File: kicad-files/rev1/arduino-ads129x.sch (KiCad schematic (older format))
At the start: 229 parts

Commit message: choose Zener and resettable fuse values
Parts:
- D?: value ZENER -> MMSZ27T1G; footprint (none) -> SOD-123
- TH?: value Resetable Fuse -> MINIASMDC050F-2; footprint (none) -> SM1812
- TH?: value PTC -> PTS181260V014; footprint (none) -> SM1812
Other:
- moved on the sheet: TH?
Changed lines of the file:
@@
-EESchema Schematic File Version 2  date Sun 09 Jun 2013 01:11:04 PM CEST
+EESchema Schematic File Version 2  date Fri 14 Jun 2013 02:24:15 AM UTC
 LIBS:power
 LIBS:device
@@
 Sheet 1 1
 Title ""
-Date "9 jun 2013"
+Date "14 jun 2013"
 Rev ""
 Comp ""
@@
 Connection ~ 19100 1900
 Wire Wire Line
-	19250 1900 19100 1900
+	19300 1900 19100 1900
 Wire Wire Line
 	19100 1900 18850 1900
@@
 	29050 29250 29050 29850
 Wire Wire Line
-	19750 1900 19900 1900
+	19800 1900 19900 1900
 Wire Wire Line
 	38750 1800 38750 2000
@@
 P 19100 2100
 F 0 "D?" H 19100 2200 50  0000 C CNN
-F 1 "ZENER" H 19100 2000 40  0000 C CNN
+F 1 "MMSZ27T1G" H 19100 2000 40  0000 C CNN
+F 2 "SOD-123" H 19100 2100 60  0001 C CNN
 	1    19100 2100
 	0    -1   -1   0
@@
 L THERMISTOR TH?
 U 1 1 51975BAD
-P 19500 1900
-F 0 "TH?" V 19600 1950 50  0000 C CNN
-F 1 "PTC" V 19400 1900 50  0000 C CNN
-	1    19500 1900
+P 19550 1900
+F 0 "TH?" V 19650 1950 50  0000 C CNN
+F 1 "PTS181260V014" V 19450 1900 50  0000 C CNN
+F 2 "SM1812" H 19550 1900 60  0001 C CNN
+	1    19550 1900
 	0    -1   -1   0
 $EndComp
@@
 P 45550 3200
 F 0 "TH?" V 45650 3250 50  0000 C CNN
-F 1 "Resetable Fuse" V 45450 3200 50  0000 C CNN
+F 1 "MINIASMDC050F-2" V 45450 3200 50  0000 C CNN
+F 2 "SM1812" H 45550 3200 60  0001 C CNN
 	1    45550 3200
 	0    1    1    0

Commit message: Added 6V preregulator
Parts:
- added C? (x2): 100nF, symbol C
- added U?: L78L06ACUTR, SOT89, symbol 7805
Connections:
- net labels added: 6V_ISO
- wire segments 1264 -> 989
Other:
- note added: "(Limits maximum voltage if a downstream regulator fails)"
- note added: "6V PREREGULATOR"

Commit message: annotate component numbers, add power flags and NCs
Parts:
- gave numbers to parts that had none: 232
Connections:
- wire segments 989 -> 1000
- no-connect marks 6 -> 57

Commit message: hook up remaining SAM3X pins
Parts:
- added R59: R, symbol R
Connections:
- net labels removed: 5V_IN, GND_IN
- wire segments 1000 -> 1007
- no-connect marks 57 -> 58

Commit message: remove extra PWRFLAG; ERC now passes
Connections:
- wire segments 1007 -> 1006

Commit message: replace preregulator with crowbar circuits
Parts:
- removed U4: L78L06ACUTR, SOT89, symbol 7805
- added 10k1, R64: 10k, symbol R
- added R60, R61: 68, symbol R
- added R62: 19.6k, symbol R
- added R63: 8.45k, symbol R
- added U14, U4: BT1308W-600D, symbol TRIAC
- added U15, U16: TL431BIDBZR, symbol TL431LP
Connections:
- net labels removed: 6V_ISO
- wire segments 1006 -> 1028
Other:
- note added: "3.8V Crowbar circuit"
- note added: "5.5V Crowbar circuit"
- note removed: "(Limits maximum voltage if a downstream regulator fails)"
- note removed: "6V PREREGULATOR"
- moved on the sheet: C41, C42, C44, C45, C49, C52, C54, C56, C57, C58, C59, C62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

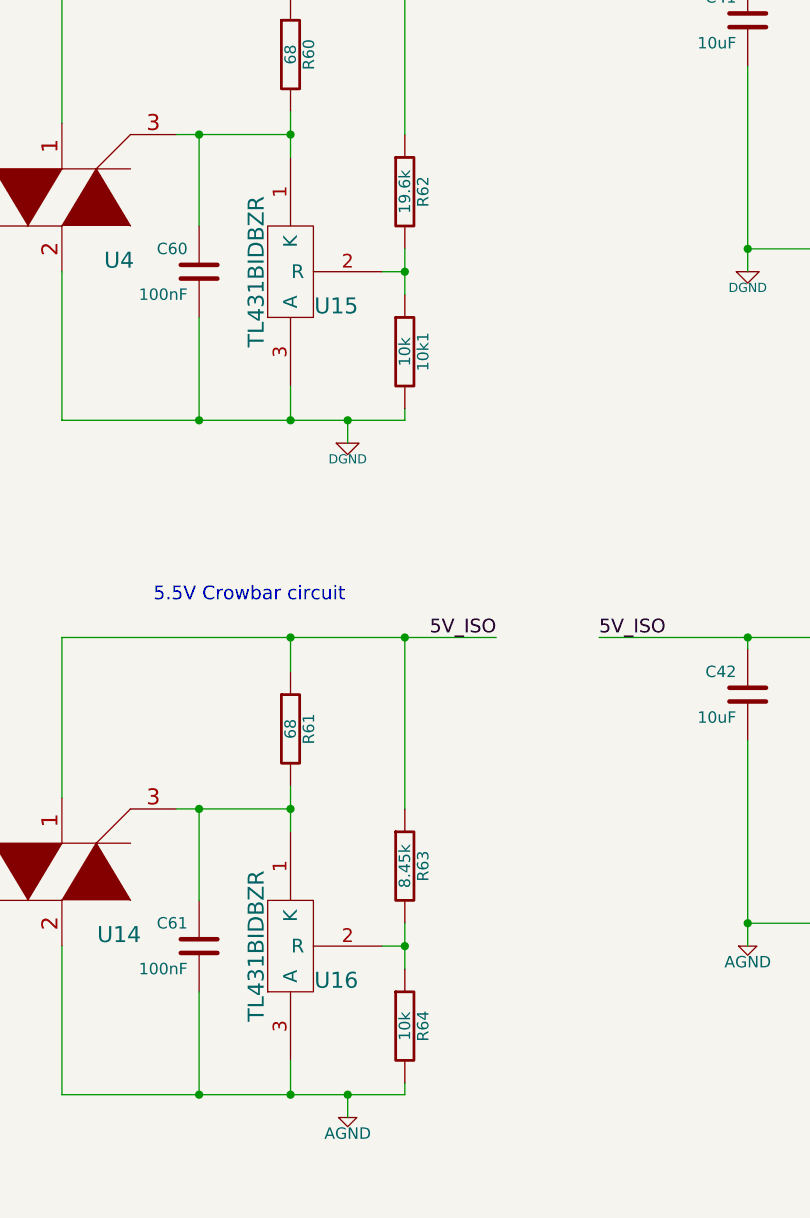
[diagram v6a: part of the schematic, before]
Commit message: swap resistors in crowbar circuits
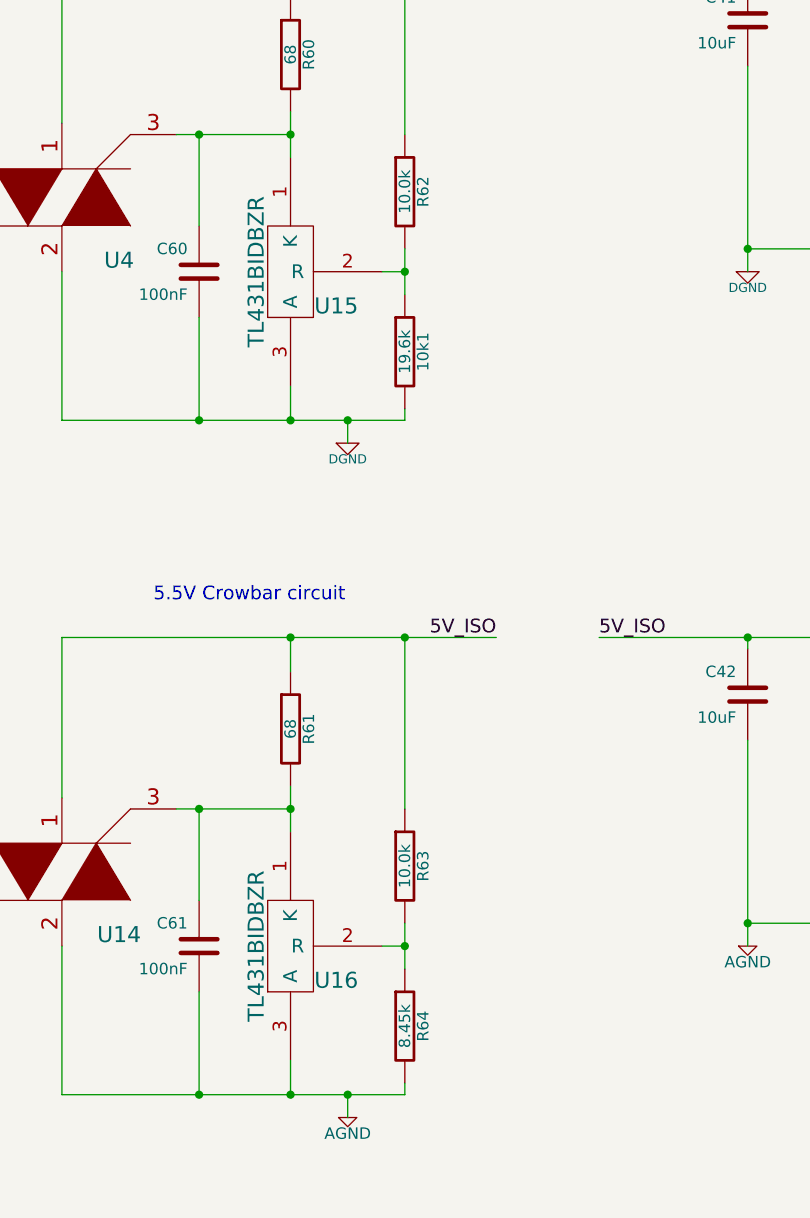
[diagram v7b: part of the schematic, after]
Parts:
- 10k1: value 10k -> 19.6k
- R62: value 19.6k -> 10.0k
- R63: value 8.45k -> 10.0k
- R64: value 10k -> 8.45k
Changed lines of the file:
@@
-EESchema Schematic File Version 2  date Sat 15 Jun 2013 02:21:45 AM UTC
+EESchema Schematic File Version 2  date Sat 15 Jun 2013 03:09:59 AM UTC
 LIBS:power
 LIBS:device
@@
 P 16100 6450
 F 0 "R62" V 16180 6450 50  0000 C CNN
-F 1 "19.6k" V 16100 6450 50  0000 C CNN
+F 1 "10.0k" V 16100 6450 50  0000 C CNN
 	1    16100 6450
 	1    0    0    -1
@@
 P 16100 7150
 F 0 "10k1" V 16180 7150 50  0000 C CNN
-F 1 "10k" V 16100 7150 50  0000 C CNN
+F 1 "19.6k" V 16100 7150 50  0000 C CNN
 	1    16100 7150
 	1    0    0    -1
@@
 P 16100 10100
 F 0 "R64" V 16180 10100 50  0000 C CNN
-F 1 "10k" V 16100 10100 50  0000 C CNN
+F 1 "8.45k" V 16100 10100 50  0000 C CNN
 	1    16100 10100
 	1    0    0    -1
@@
 P 16100 9400
 F 0 "R63" V 16180 9400 50  0000 C CNN
-F 1 "8.45k" V 16100 9400 50  0000 C CNN
+F 1 "10.0k" V 16100 9400 50  0000 C CNN
 	1    16100 9400
 	1    0    0    -1

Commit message: Labeled Ferrite Beads/INDUCTORs as MH2029-221Y
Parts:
- added L21: MH2029-221Y, symbol INDUCTOR
- L1, L10, L11, L12, L13, L14, L15, L16, L17, L18, L2, L3, L4, L5, L6, L9: value INDUCTOR -> MH2029-221Y
- L20: value FERRITE BEAD -> MH2029-221Y
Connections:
- wire segments 1028 -> 1029
